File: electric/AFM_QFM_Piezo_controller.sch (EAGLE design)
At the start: 49 parts, among them U1 LTC3260EMSE#PBF, U2 AD5696RARUZ-RL7RU_16_ADI-M, U3 LM324KAD

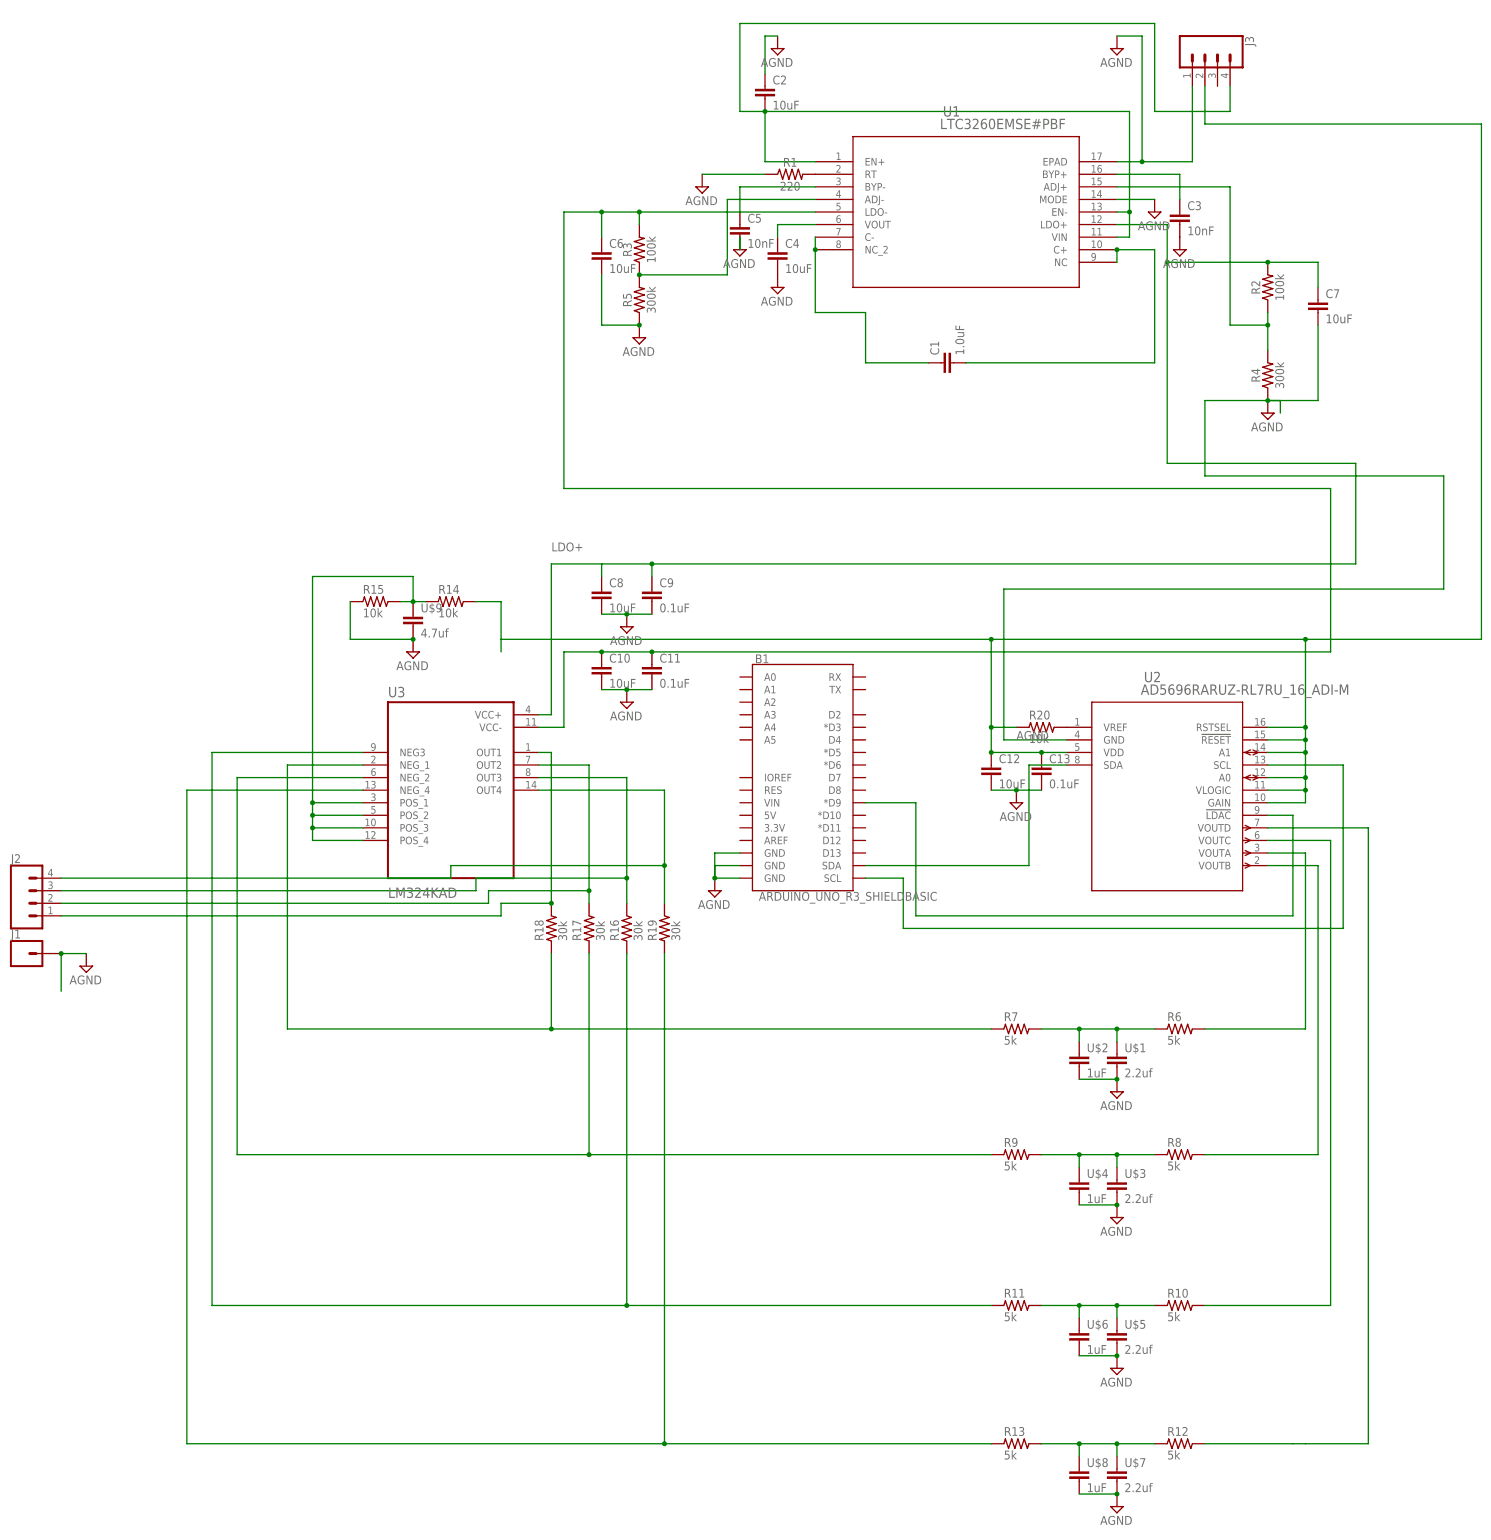
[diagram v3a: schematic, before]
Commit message: Updated to boards. Changes reflects fixes needed to PCBWay boards
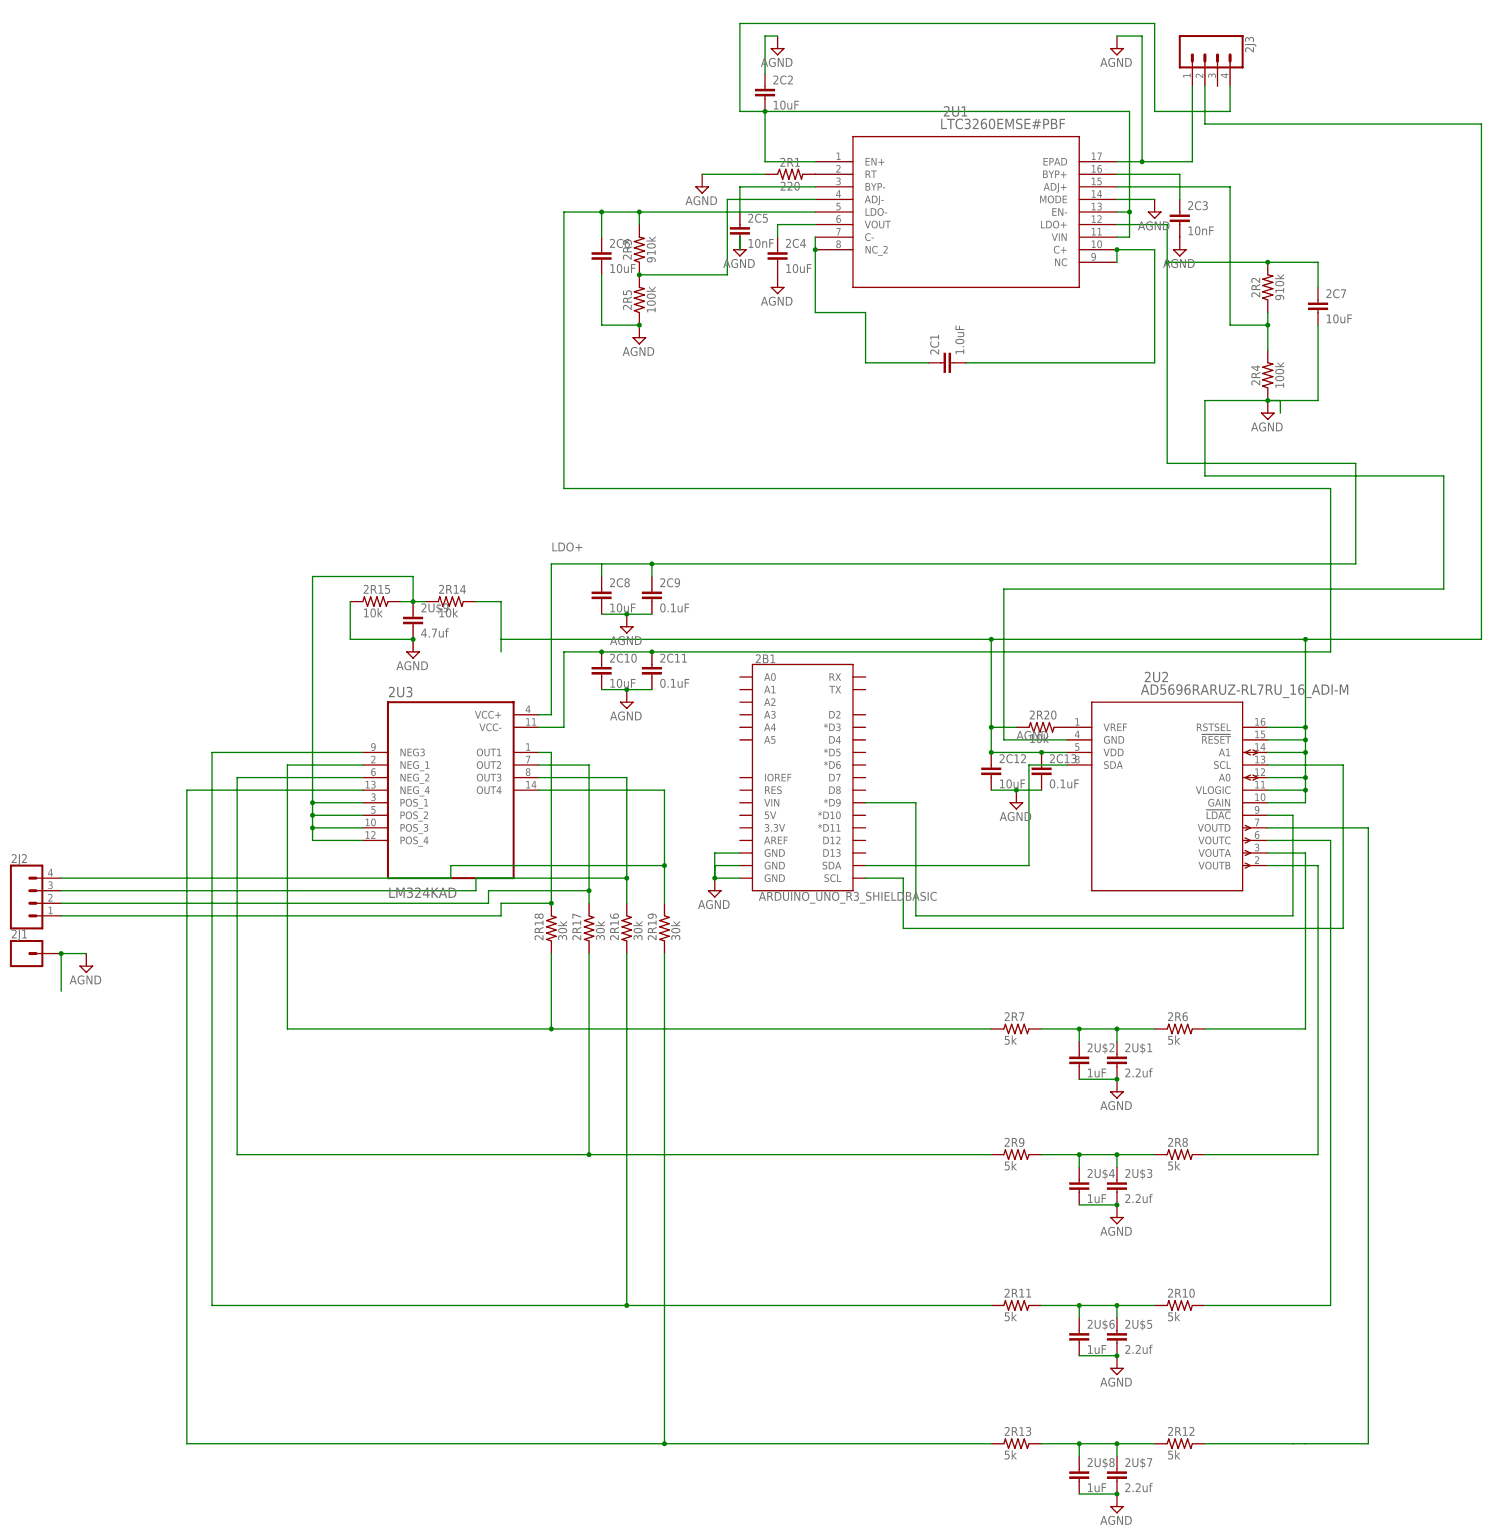
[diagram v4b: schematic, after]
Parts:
- 2R2, 2R3: value 100k -> 910k
- 2R4, 2R5: value 300k -> 100k
- renumbered B1 to 2B1, C1 to 2C1, C10 to 2C10, C11 to 2C11, C12 to 2C12, C13 to 2C13, C2 to 2C2, C3 to 2C3, C4 to 2C4, C5 to 2C5, C6 to 2C6, C7 to 2C7, C8 to 2C8, C9 to 2C9, J1 to 2J1, J2 to 2J2, J3 to 2J3, R1 to 2R1, R10 to 2R10, R11 to 2R11, R12 to 2R12, R13 to 2R13, R14 to 2R14, R15 to 2R15, R16 to 2R16, R17 to 2R17, R18 to 2R18, R19 to 2R19, R2 to 2R2, R20 to 2R20, R3 to 2R3, R4 to 2R4, R5 to 2R5, R6 to 2R6, R7 to 2R7, R8 to 2R8, R9 to 2R9, U$1 to 2U$1, U$2 to 2U$2, U$3 to 2U$3, U$4 to 2U$4, U$5 to 2U$5, U$6 to 2U$6, U$7 to 2U$7, U$8 to 2U$8, U$9 to 2U$9, U1 to 2U1, U2 to 2U2, U3 to 2U3
